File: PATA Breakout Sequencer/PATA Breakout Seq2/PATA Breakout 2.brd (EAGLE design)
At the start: 60 x 100 mm, 57 parts, among them IC1 74HC165N, IC2 74HC165N, IC3 74HC165N, IC4 74HC165N, IC5 74HC165N

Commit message: Finished routing
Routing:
- net G2: track 78.6 -> 80.5 mm
- net B1: track 45.1 -> 46.0 mm
- net D3: track 49.1 -> 48.2 mm
- net H2: track 77.6 -> 78.4 mm
- net E3: track 64.9 -> 64.1 mm
- net F3: track 62.4 -> 63.0 mm
- net F1: track 59.7 -> 60.3 mm

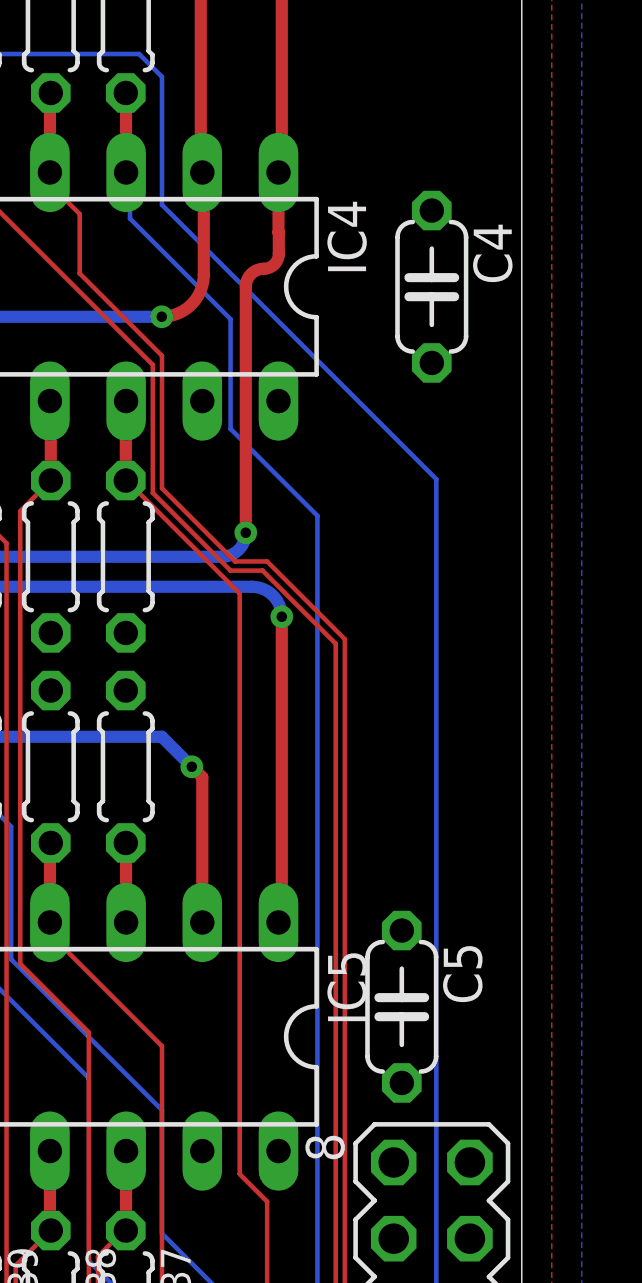
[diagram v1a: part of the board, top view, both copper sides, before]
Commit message: Update PATA Breakout 2.brd
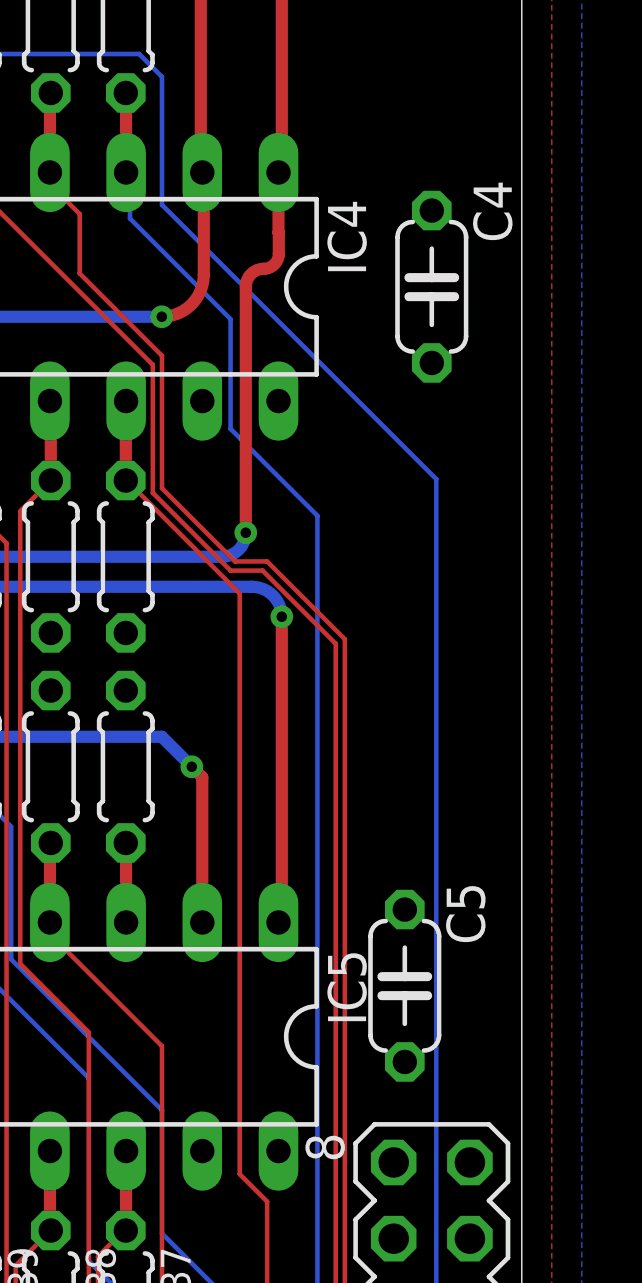
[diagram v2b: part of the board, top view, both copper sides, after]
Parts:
- moved C5 0.71 mm to (56.1, 26.7)
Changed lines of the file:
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@@
 <attribute name="NAME" x="1.603" y="24.841" size="1.27" layer="25" ratio="10" rot="R90"/>
 <attribute name="SPICEPREFIX" value="C" x="3" y="27" size="1.778" layer="27" rot="R90" display="off"/>
-<attribute name="VALUE" x="5.667" y="24.841" size="1.27" layer="27" ratio="10" rot="R90"/>
+<attribute name="VALUE" x="1.667" y="28.141" size="1.27" layer="27" ratio="10" rot="R90"/>
 </element>
 <element name="C2" library="rcl" library_urn="urn:adsk.eagle:library:334" package="C050-024X044" package3d_urn="urn:adsk.eagle:package:23643/1" value="4.7uF" x="3" y="50" smashed="yes" rot="R90">
 <attribute name="NAME" x="1.603" y="47.841" size="1.27" layer="25" ratio="10" rot="R90"/>
 <attribute name="SPICEPREFIX" value="C" x="3" y="50" size="1.778" layer="27" rot="R90" display="off"/>
-<attribute name="VALUE" x="5.667" y="47.841" size="1.27" layer="27" ratio="10" rot="R90"/>
+<attribute name="VALUE" x="1.667" y="51.141" size="1.27" layer="27" ratio="10" rot="R90"/>
 </element>
 <element name="C3" library="rcl" library_urn="urn:adsk.eagle:library:334" package="C050-024X044" package3d_urn="urn:adsk.eagle:package:23643/1" value="4.7uF" x="17" y="68" smashed="yes" rot="R90">
 <attribute name="NAME" x="15.603" y="65.841" size="1.27" layer="25" ratio="10" rot="R90"/>
 <attribute name="SPICEPREFIX" value="C" x="17" y="68" size="1.778" layer="27" rot="R90" display="off"/>
-<attribute name="VALUE" x="19.667" y="65.841" size="1.27" layer="27" ratio="10" rot="R90"/>
+<attribute name="VALUE" x="15.667" y="68.941" size="1.27" layer="27" ratio="10" rot="R90"/>
 </element>
 <element name="C4" library="rcl" library_urn="urn:adsk.eagle:library:334" package="C050-024X044" package3d_urn="urn:adsk.eagle:package:23643/1" value="4.7uF" x="57" y="50" smashed="yes" rot="R270">
-<attribute name="NAME" x="58.397" y="52.159" size="1.27" layer="25" ratio="10" rot="R270"/>
+<attribute name="NAME" x="58.397" y="53.559" size="1.27" layer="25" ratio="10" rot="R270"/>
 <attribute name="SPICEPREFIX" value="C" x="57" y="50" size="1.778" layer="27" rot="R270" display="off"/>
-<attribute name="VALUE" x="54.333" y="52.159" size="1.27" layer="27" ratio="10" rot="R270"/>
+<attribute name="VALUE" x="58.333" y="49.959" size="1.27" layer="27" ratio="10" rot="R270"/>
 </element>
-<element name="C5" library="rcl" library_urn="urn:adsk.eagle:library:334" package="C050-024X044" package3d_urn="urn:adsk.eagle:package:23643/1" value="4.7uF" x="56" y="26" smashed="yes" rot="R270">
-<attribute name="NAME" x="57.397" y="28.159" size="1.27" layer="25" ratio="10" rot="R270"/>
-<attribute name="SPICEPREFIX" value="C" x="56" y="26" size="1.778" layer="27" rot="R270" display="off"/>
-<attribute name="VALUE" x="53.333" y="28.159" size="1.27" layer="27" ratio="10" rot="R270"/>
+<element name="C5" library="rcl" library_urn="urn:adsk.eagle:library:334" package="C050-024X044" package3d_urn="urn:adsk.eagle:package:23643/1" value="4.7uF" x="56.1" y="26.7" smashed="yes" rot="R270">
+<attribute name="NAME" x="57.497" y="30.159" size="1.27" layer="25" ratio="10" rot="R270"/>
+<attribute name="SPICEPREFIX" value="C" x="56.1" y="26.7" size="1.778" layer="27" rot="R270" display="off"/>
+<attribute name="VALUE" x="57.433" y="27.159" size="1.27" layer="27" ratio="10" rot="R270"/>
 </element>
 </elements>

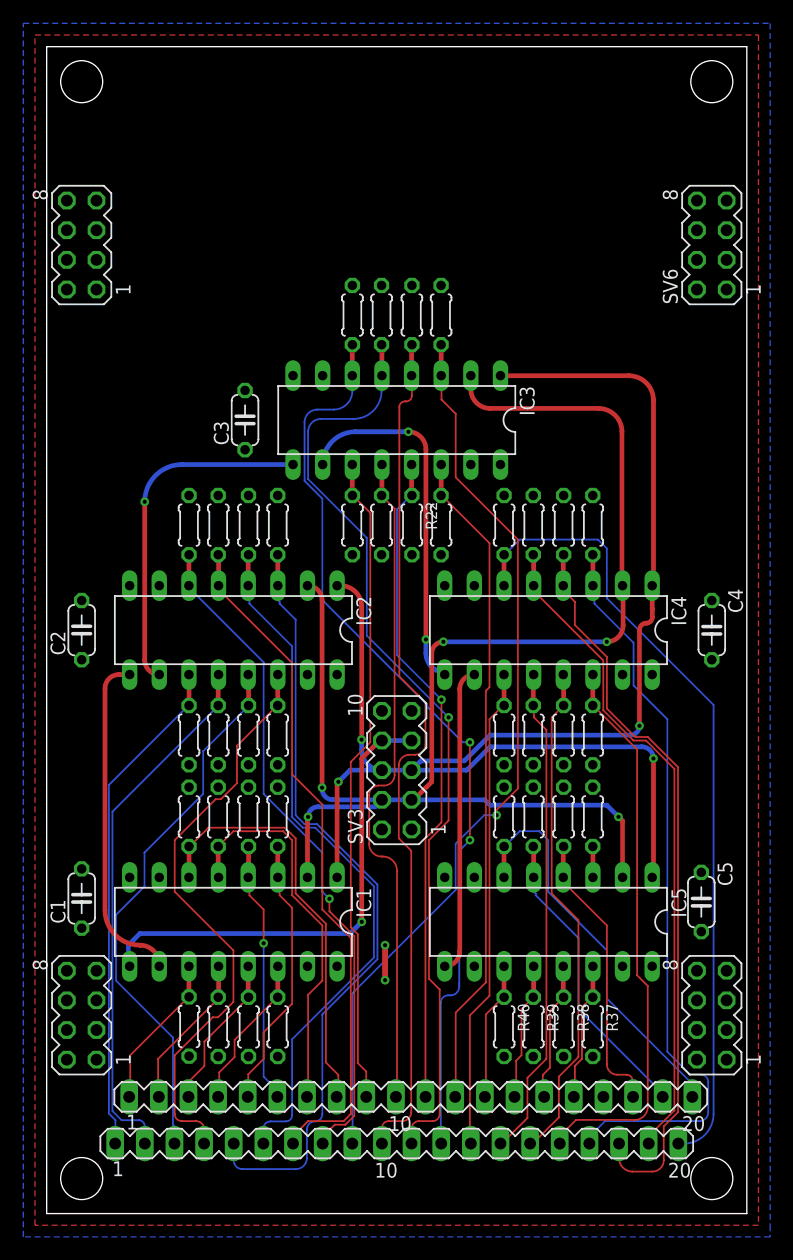
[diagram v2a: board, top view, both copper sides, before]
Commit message: Finished top board - ran DRC
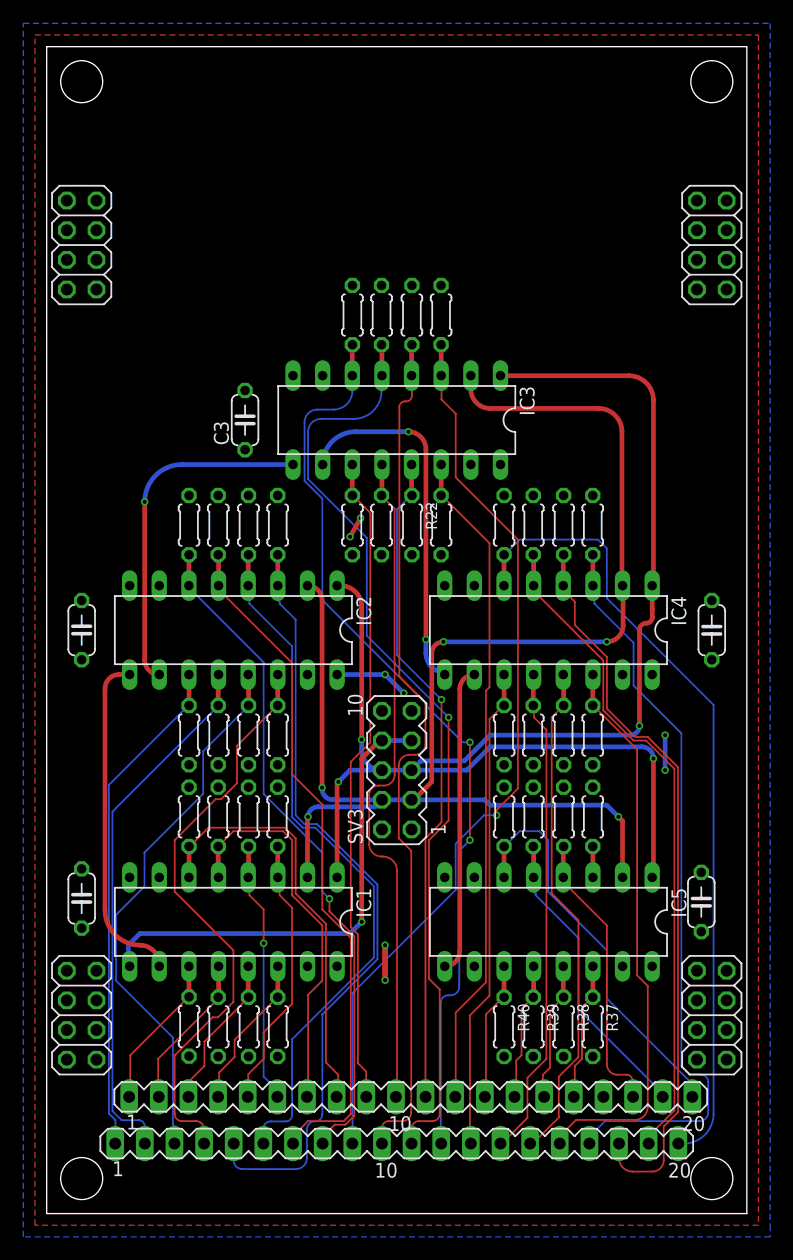
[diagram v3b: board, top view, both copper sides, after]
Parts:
- SV4, SV5, SV6, SV7: device con-lstb:MA04-2 -> pinhead:2X04
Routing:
- net VCC: track 0.00 -> 9.38 mm, vias 0 -> 4
- net GND: track 3.00 -> 4.84 mm, vias 2 -> 4

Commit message: cleanup
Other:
- board text added: "Koltin Kosik-Harvey March 7 / 2019"
- board text added: "PATA Sequencer Breakout BOTTOM"
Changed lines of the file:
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@@
 <hole x="3" y="97" drill="3.6"/>
 <hole x="57" y="97" drill="3.6"/>
+<text x="9" y="84" size="1.778" layer="21">PATA Sequencer
+Breakout
+BOTTOM</text>
+<text x="31" y="84" size="1.778" layer="21">Koltin Kosik-Harvey
+March 7 / 2019</text>
+<wire x1="6" y1="12" x2="6" y2="8" width="0.1524" layer="21"/>
+<wire x1="26" y1="12" x2="26" y2="8" width="0.1524" layer="21"/>
+<wire x1="46" y1="12" x2="46" y2="8" width="0.1524" layer="21"/>
+<wire x1="45" y1="8" x2="45" y2="4" width="0.1524" layer="21"/>
+<wire x1="25" y1="8" x2="25" y2="4" width="0.1524" layer="21"/>
+<wire x1="4" y1="8" x2="4" y2="4" width="0.1524" layer="21"/>
 </plain>
 <attributes>
@@
 </drawing>
 <compatibility>
+<note version="6.3" minversion="6.2.2" severity="warning">
+Since Version 6.2.2 text objects can contain more than one line,
+which will not be processed correctly with this version.
+</note>
 <note version="8.2" severity="warning">
 Since Version 8.2, EAGLE supports online libraries. The ids
